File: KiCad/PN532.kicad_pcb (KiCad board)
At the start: 2 copper layers, 40 x 40 mm, 56 parts, among them J1 Bell, J2 Header, J3 SPOX, SW1 TAMPER, U1 PN532, U2 QR, U3 QR, Y1 27.12MHz

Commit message: Tweak
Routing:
- net Net-(R11-Pad2): track 26.9 -> 20.4 mm
- net GND: track 140.9 -> 134.4 mm

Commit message: Never ending tinkering
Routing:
- net Net-(C9-Pad1): track 9.60 -> 8.56 mm
- net Net-(C8-Pad1): track 8.91 -> 9.64 mm

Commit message: More cut down.
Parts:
- removed J2: Header, RevK:PinHeader_1x04_P2.54mm_Vertical
- J3: footprint RevK:Molex_MiniSPOX_H4RA -> RevK:Molex_MiniSPOX_H4V
- SW1: footprint RevK:SW_PUSH_6mm_PTH_SMD -> RevK:SW_PUSH_6mm_SMD
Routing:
- net GND: track 134.4 -> 128.5 mm, vias 13 -> 14
- net +5V: track 33.8 -> 30.6 mm
- net Net-(J3-Pad4): track 11.5 -> 8.42 mm
- net Net-(J3-Pad3): track 6.22 -> 3.11 mm
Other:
- board text added: "PN532 HSU 3.3V"

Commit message: Tidy up
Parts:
- moved U2 0.90 mm to (89.4, 110.6)
- moved U3 0.90 mm to (89.4, 110.6)
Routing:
- net GND: track 128.5 -> 126.1 mm
- net Net-(D3-Pad2): track 16.4 -> 17.4 mm
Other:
- board text added: "+"
- board text added: "-"
- board text added: "<"
- board text added: ">"
- board text removed: "GND"
- board text removed: "RX"
- board text removed: "TX"
- board text removed: "VCC"

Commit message: Documentation
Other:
- board text removed: "2 layer 35 micron copper weight FR4 0.8mm ENIG finish Green resist, white silkscreen"
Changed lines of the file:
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@@
       (primitives
         (gr_line (start 0 0) (end 12 0) (width 0.5))
-    (gr_arc (start 12 0) (mid 16.9411 2.041622) (end 18.999954 6.975566) (width 0.5))
+    (gr_arc (start 12 0) (mid 16.932437 2.033006) (end 18.999824 6.951132) (width 0.5))
         (gr_line (start 19 7) (end 19 31) (width 0.5))
-    (gr_arc (start 19 31) (mid 16.958378 35.9411) (end 12.024434 37.999954) (width 0.5))
+    (gr_arc (start 19 31) (mid 16.966994 35.932437) (end 12.048868 37.999824) (width 0.5))
         (gr_line (start 12 38) (end -12 38) (width 0.5))
-    (gr_arc (start -12 38) (mid -16.9411 35.958378) (end -18.999954 31.024434) (width 0.5))
+    (gr_arc (start -12 38) (mid -16.932437 35.966994) (end -18.999824 31.048868) (width 0.5))
         (gr_line (start -19 31) (end -19 7) (width 0.5))
     (gr_arc (start -19 7) (mid -17.242642 2.75736) (end -13.000002 1) (width 0.5))
@@
     (gr_arc (start 12 1) (mid 16.24264 2.757358) (end 18 6.999998) (width 0.5))
         (gr_line (start 18 7) (end 18 31) (width 0.5))
-    (gr_arc (start 18 31) (mid 16.253733 35.231519) (end 12.031416 36.999918) (width 0.5))
+    (gr_arc (start 18 31) (mid 16.261112 35.224088) (end 12.052359 36.999772) (width 0.5))
         (gr_line (start 12 37) (end -12 37) (width 0.5))
     (gr_arc (start -12 37) (mid -16.24264 35.242642) (end -18 31.000002) (width 0.5))
         (gr_line (start -18 31) (end -18 7) (width 0.5))
-    (gr_arc (start -18 7) (mid -16.544779 3.473735) (end -13.026183 2.00007) (width 0.5))
+    (gr_arc (start -18 7) (mid -16.547857 3.476831) (end -13.034913 2.000123) (width 0.5))
         (gr_line (start -13 2) (end -3 2) (width 0.5))
         (gr_line (start -1 0) (end 0 0) (width 0.5))
@@
       (primitives
         (gr_line (start -12 0) (end 0 0) (width 0.5))
-    (gr_arc (start -18.999989 6.987787) (mid -16.94975 2.050255) (end -12.01222 0.000009) (width 0.5))
+    (gr_arc (start -18.999989 6.987787) (mid -16.95838 2.0589) (end -12.036652 0.000094) (width 0.5))
         (gr_line (start -19 31) (end -19 7) (width 0.5))
-    (gr_arc (start -12.012213 37.999989) (mid -16.949745 35.94975) (end -18.999991 31.01222) (width 0.5))
+    (gr_arc (start -12.012213 37.999989) (mid -16.9411 35.95838) (end -18.999906 31.036652) (width 0.5))
         (gr_line (start 12 38) (end -12 38) (width 0.5))
-    (gr_arc (start 18.999989 31.012213) (mid 16.94975 35.949745) (end 12.01222 37.999991) (width 0.5))
+    (gr_arc (start 18.999989 31.012213) (mid 16.95838 35.9411) (end 12.036652 37.999906) (width 0.5))
         (gr_line (start 19 7) (end 19 31) (width 0.5))
-    (gr_arc (start 13.000002 1) (mid 17.235229 2.74996) (end 18.999962 6.979053) (width 0.5))
+    (gr_arc (start 13.000002 1) (mid 17.224089 2.738887) (end 18.999772 6.947639) (width 0.5))
         (gr_line (start -12 1) (end 13 1) (width 0.5))
     (gr_arc (start -18 6.999998) (mid -16.24264 2.757358) (end -12 1) (width 0.5))
@@
     (gr_arc (start 18 31.000002) (mid 16.24264 35.242642) (end 12 37) (width 0.5))
         (gr_line (start 18 7) (end 18 31) (width 0.5))
-    (gr_arc (start 13.017453 2.00003) (mid 16.532447 3.461381) (end 17.999931 6.973819) (width 0.5))
+    (gr_arc (start 13.017453 2.00003) (mid 16.532446 3.46138) (end 17.999931 6.973817) (width 0.5))
         (gr_line (start 2 2) (end 13 2) (width 0.5))
         (gr_line (start 0 0) (end 1 0) (width 0.5))
@@
     (effects (font (size 1 1) (thickness 0.15)) (justify right))
   )
-  (gr_text "-" (at 96.25 110.9 90) (layer "F.SilkS")
-    (effects (font (size 1 1) (thickness 0.15)) (justify right))
-  )
-  (gr_text "+" (at 98.75 110.9 90) (layer "F.SilkS")
-    (effects (font (size 1 1) (thickness 0.15)) (justify right))
+  (gr_text "-" (at 96.25 111.75 180) (layer "F.SilkS")
+    (effects (font (size 1 1) (thickness 0.15)))
+  )
+  (gr_text "+" (at 98.75 111.75 180) (layer "F.SilkS")
+    (effects (font (size 1 1) (thickness 0.15)))
   )
   (gr_text "Bell" (at 113.9 106 90) (layer "F.SilkS")
@@
     (effects (font (size 1 1) (thickness 0.15)))
   )
-  (gr_text "2 layer\n35 micron copper weight\nFR4 0.8mm\nENIG finish\nGreen resist, white silkscreen" (at 137.1 100.8) (layer "Dwgs.User")
-    (effects (font (size 2 2) (thickness 0.3)) (justify left))
-  )
   (gr_text "P30" (at 88.5 100) (layer "B.Fab")

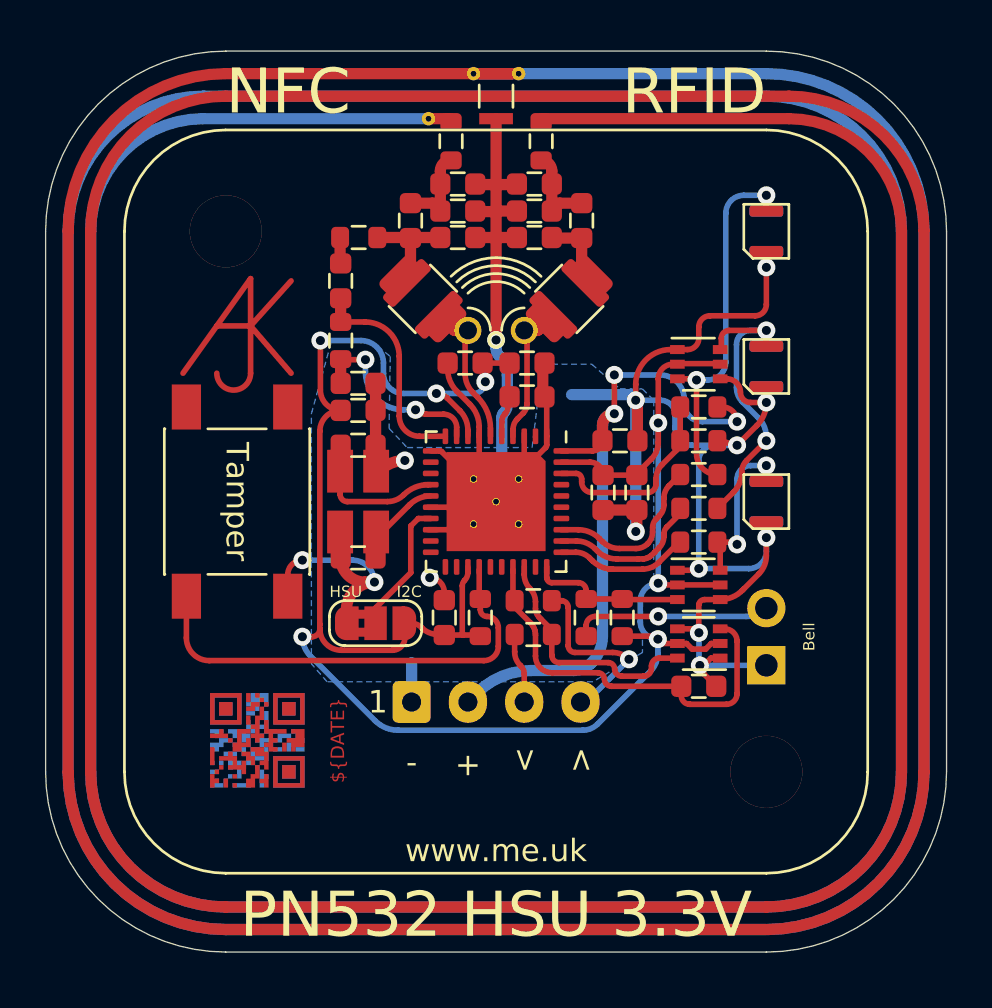
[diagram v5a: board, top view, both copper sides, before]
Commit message: Cleaner up BOM
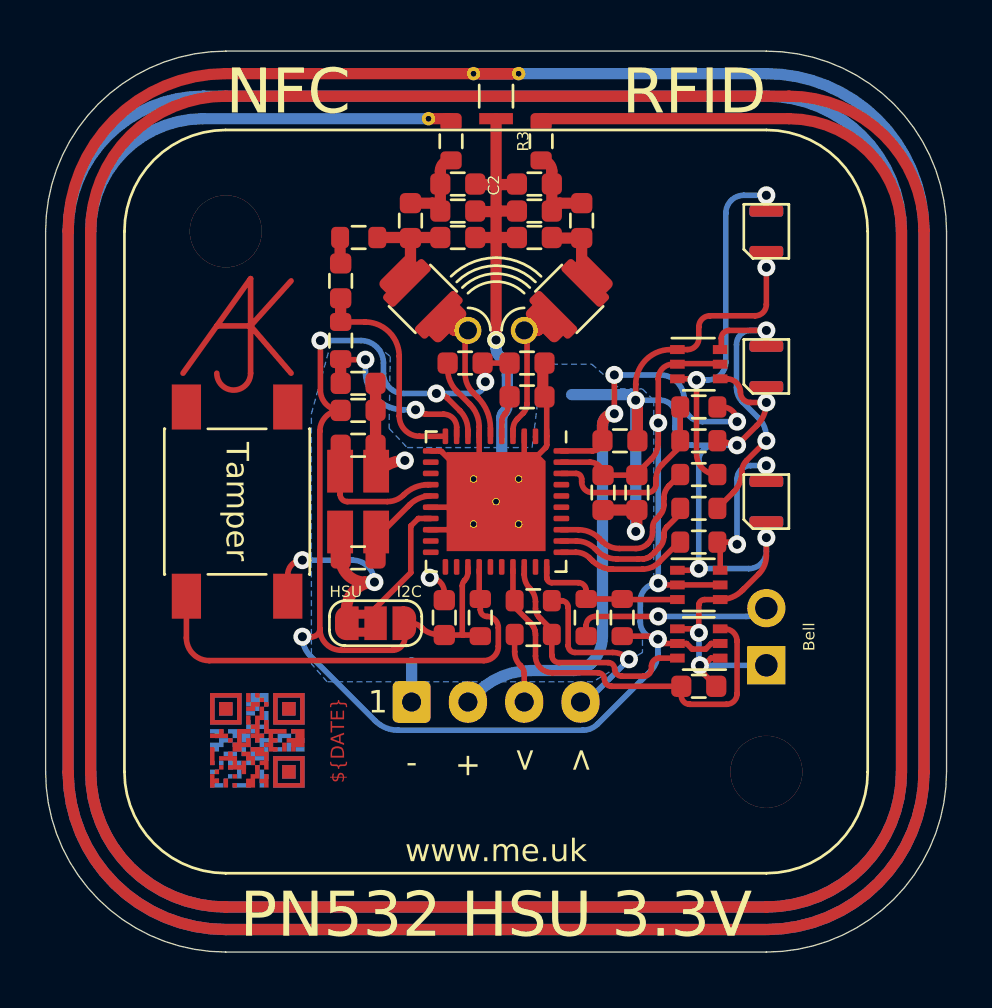
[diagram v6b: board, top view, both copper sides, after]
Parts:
- turned R3 to 90 degrees
- renumbered J3 to J2
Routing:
- net GND: track 126.1 -> 125.0 mm

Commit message: Reverse mount LEDs
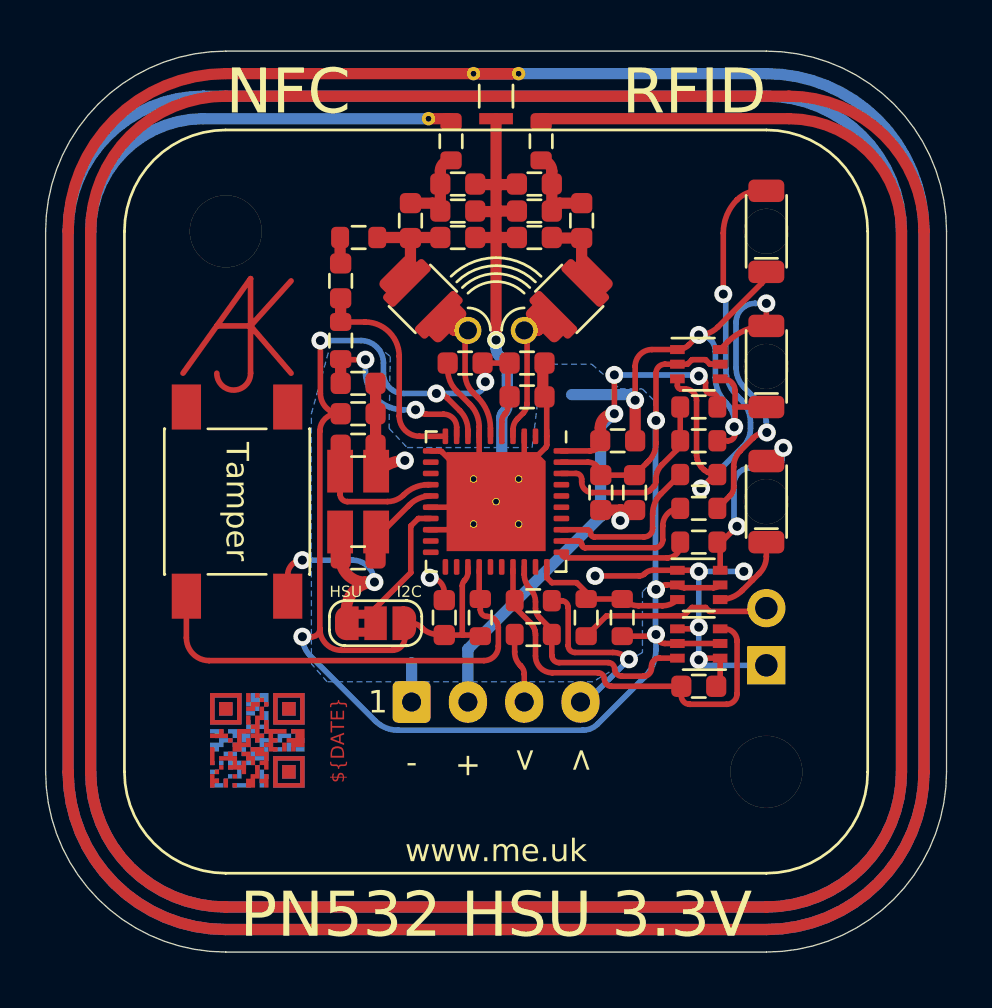
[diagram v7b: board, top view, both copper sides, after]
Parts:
- D1, D2, D3: footprint RevK:LED_Reverse -> RevK:STP_156120xx7530
- R10, R9: value 680R -> 100R
- R8: value 470R -> 100R
- moved C15 0.15 mm to (93.9, 96.1)
- moved C11 0.10 mm to (104.7, 99.6)
- moved C13 0.10 mm to (106.2, 99.6)
- moved C14 0.10 mm to (105.4, 97.3)
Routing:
- net GND: track 125.0 -> 108.2 mm
- net +5V: track 30.6 -> 26.0 mm
- net Net-(D3-Pad2): track 17.4 -> 21.9 mm
- net Net-(D2-Pad2): track 14.2 -> 14.9 mm
- net Net-(D1-Pad2): track 8.05 -> 8.65 mm
- net Net-(J1-Pad2): track 8.78 -> 8.66 mm, vias 1 -> 0
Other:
- board text removed: "Bell"

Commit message: Cleanup BOM more
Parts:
- moved C7 0.15 mm to (101.4, 95.2)
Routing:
- net (no net): track 0.00 -> 1.28 mm
- net GND: track 108.2 -> 107.0 mm
- net Net-(D2-Pad2): track 14.9 -> 15.7 mm
- net +5V: track 26.0 -> 25.3 mm
- net Net-(C17-Pad1): track 4.04 -> 3.43 mm
- net Net-(JP1-Pad2): track 5.99 -> 6.54 mm
- net +3V3: track 91.7 -> 92.3 mm
